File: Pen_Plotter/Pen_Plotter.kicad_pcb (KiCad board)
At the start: 2 copper layers, 74.8 x 35.8 mm, 36 parts, among them J1 USB4125-GF-A_REVA2, J2 PinHeader_01x05_P2.54mm_Verti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, J3 PinHeader_01x05_P2.54mm_Verti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, J4 Conn_02x03_Counter_Clockwise, J5 PinHeader_01x02_P2.54mm_Verti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, J6 PinHeader_01x02_P2.54mm_Verti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, J7 PinHeader_01x03_P2.54mm_Verti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, SW1 Switch_Tactile_Omron, SW2 Switch_Tactile_Omron, U1 ESP32-WROOM-32E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

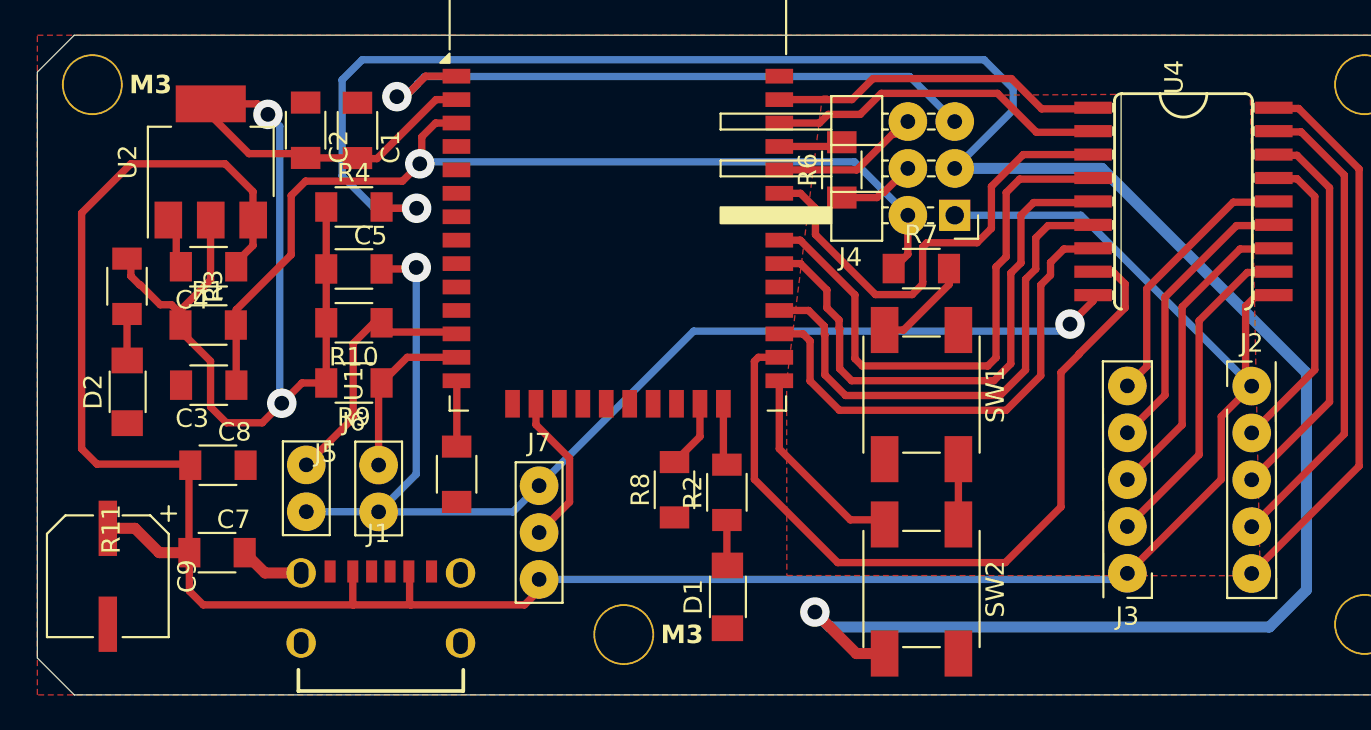
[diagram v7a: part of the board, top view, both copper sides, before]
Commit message: PCB _ TX and RX Corrected
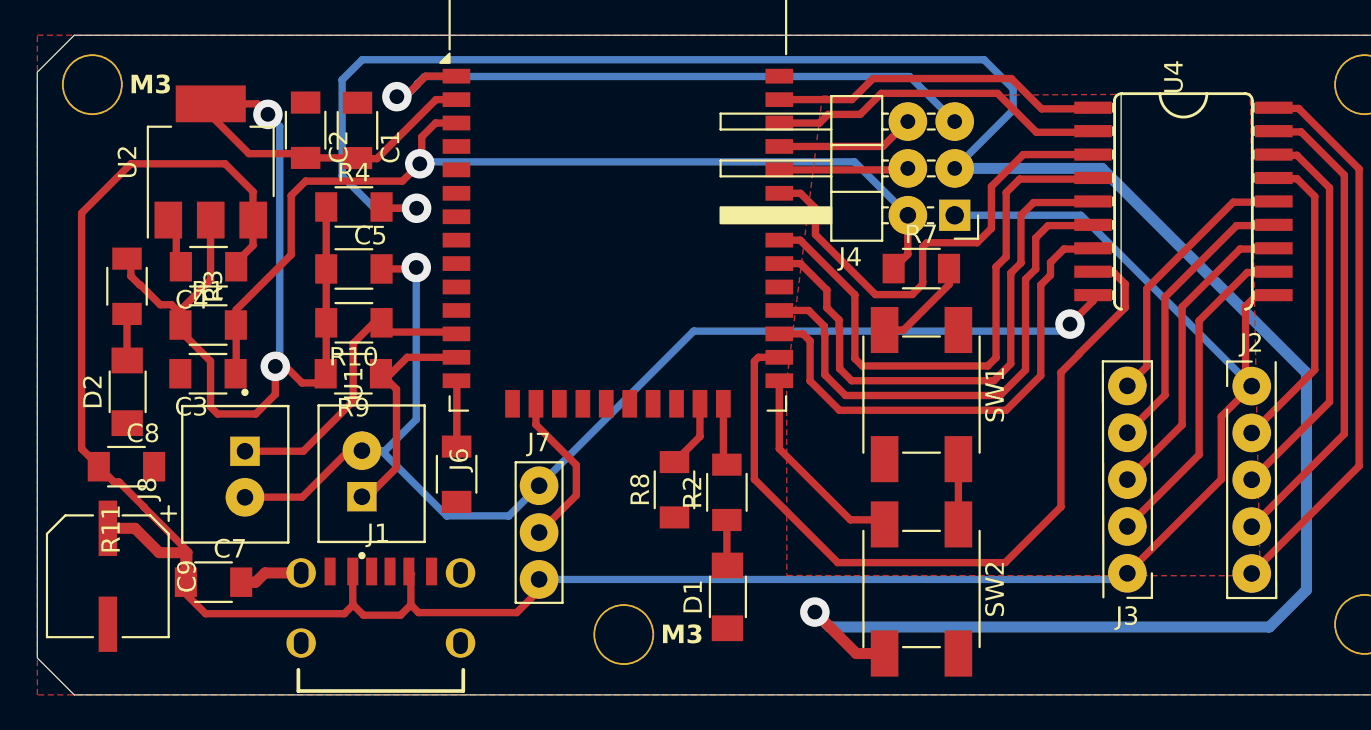
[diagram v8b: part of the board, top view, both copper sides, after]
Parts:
- removed J5: PinHeader_01x02_P2.54mm_Vertical_THT_D1.4mm, fab:PinHeader_01x02_P2.54mm_Vertical_THT_D1.4mm
- removed R6: 0, fab:R_1206
- added J8: X Lim, B2B-XH-A_LF__SN_:JST_B2B-XH-A_LF__SN_, F.Cu at (66.4, 115.8)
- C7: value C_1206 -> 0.1uF
- J6: value PinHeader_01x02_P2.54mm_Vertical_THT_D1.4mm -> X Lim; footprint fab:PinHeader_01x02_P2.54mm_Vertical_THT_D1.4mm -> B2B-XH-A_LF__SN_:JST_B2B-XH-A_LF__SN_
- R10: value R_1206 -> 10K
- SW1: value Switch_Tactile_Omron -> Reset-EN
- SW2: value Switch_Tactile_Omron -> Boot-GPIO0
- moved C8 4.96 mm to (60.5, 115.4)
- moved J6 3.57 mm to (73.8, 115.8), turned to -90 degrees
- moved C7 1.61 mm to (65.2, 121.7)
- moved C3 0.62 mm to (64.9, 110.4)
- moved R9 0.50 mm to (72.8, 110.4)
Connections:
- J4 pad 4: TX -> ESP_RX
- J4 pad 6: RX -> ESP_TX
- J6 pad 1: X Lim -> Y Lim
- U1 pad 34: RX -> ESP_RX
- U1 pad 35: TX -> ESP_TX
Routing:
- net RX: track 8.34 -> 0.00 mm
- net TX: track 7.72 -> 0.00 mm
- net ESP_TX: track 0.00 -> 7.53 mm
- net ESP_RX: track 0.00 -> 7.00 mm
- net PWR_GND: track 109.1 -> 112.7 mm
- net Y Lim: track 9.15 -> 12.4 mm
- net X Lim: track 13.9 -> 16.4 mm
- net VDD: track 69.3 -> 68.3 mm
- net EN: track 59.3 -> 58.7 mm
